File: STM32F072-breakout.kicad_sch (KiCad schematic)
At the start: 38 parts, among them J1 USB_B_Micro, J2 Conn_01x04_Pin, J3 Conn_01x30_Pin, J4 Conn_01x30_Pin, J5 Conn_01x04_Pin, SW1 SW_SPST, U1 STM32F072RBTx, U2 AMS1117-3.3, U3 MCP2551-I-SN, Y1 8MHz

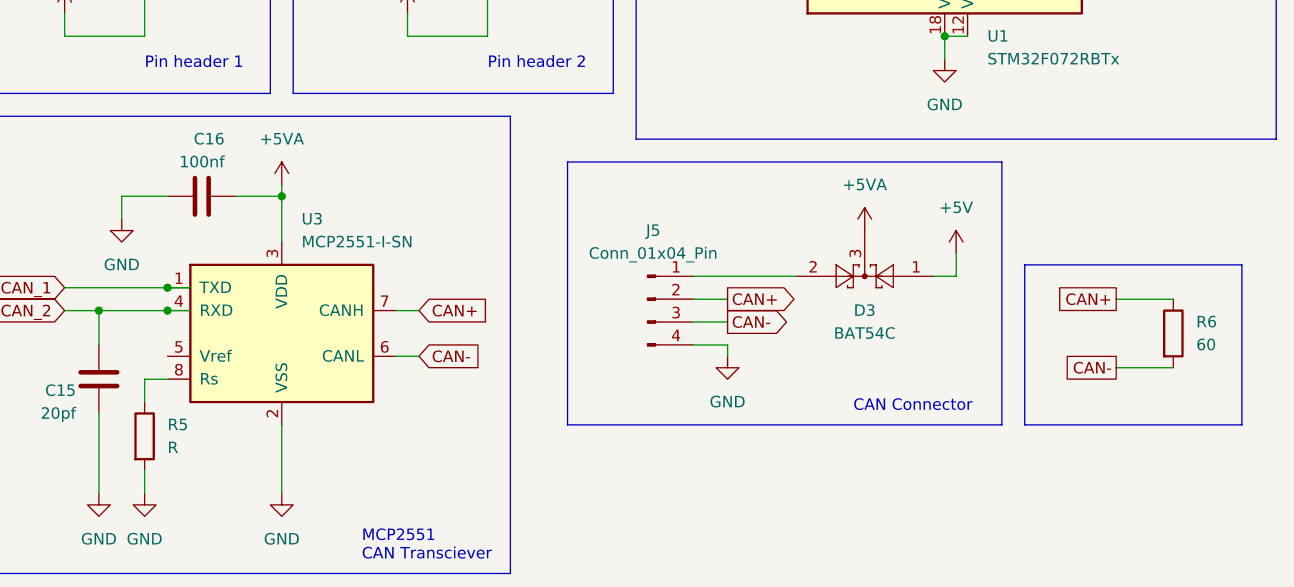
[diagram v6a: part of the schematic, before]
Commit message: fix missing CAN connection
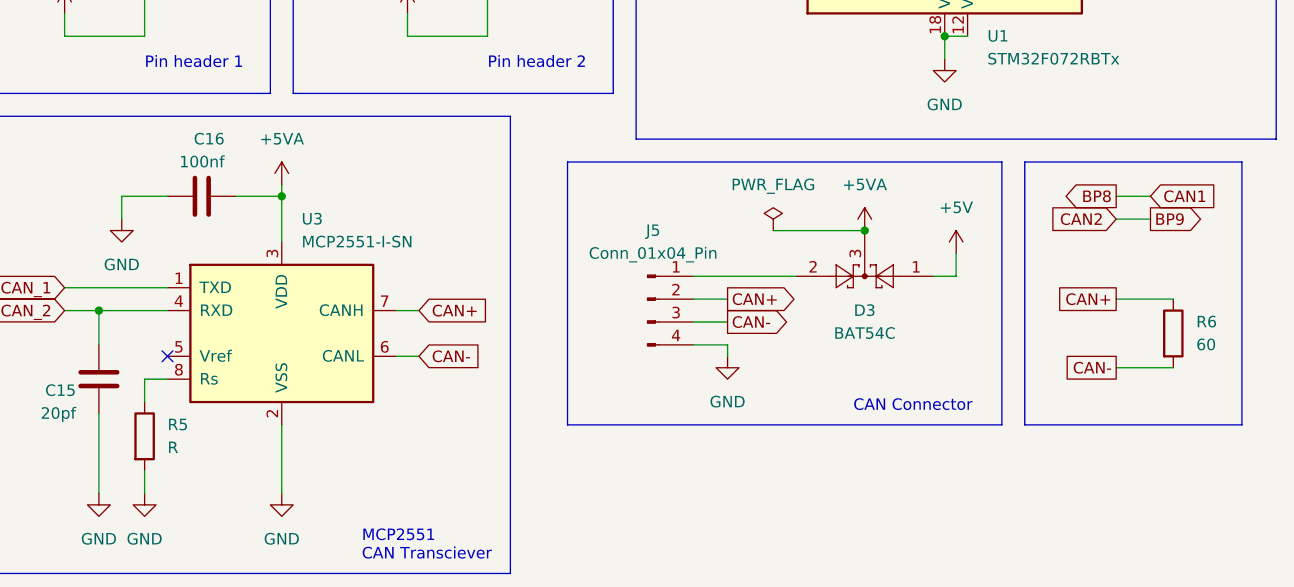
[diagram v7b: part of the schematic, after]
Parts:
- J5: footprint (none) -> Connector_PinHeader_1.00mm:PinHeader_1x04_P1.00mm_Vertical
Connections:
- no-connect marks 2 -> 3
